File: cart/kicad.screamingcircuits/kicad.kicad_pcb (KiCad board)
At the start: 4 copper layers, 100 x 64 mm, 29 parts, among them J1 Bus_TI994A_Cart, J2 Conn_01x06, U1 MCP1700-3302E_SOT23, U2 S29GL01G-128MB-Flash, U3 GigaCart_CPLD_LC4064

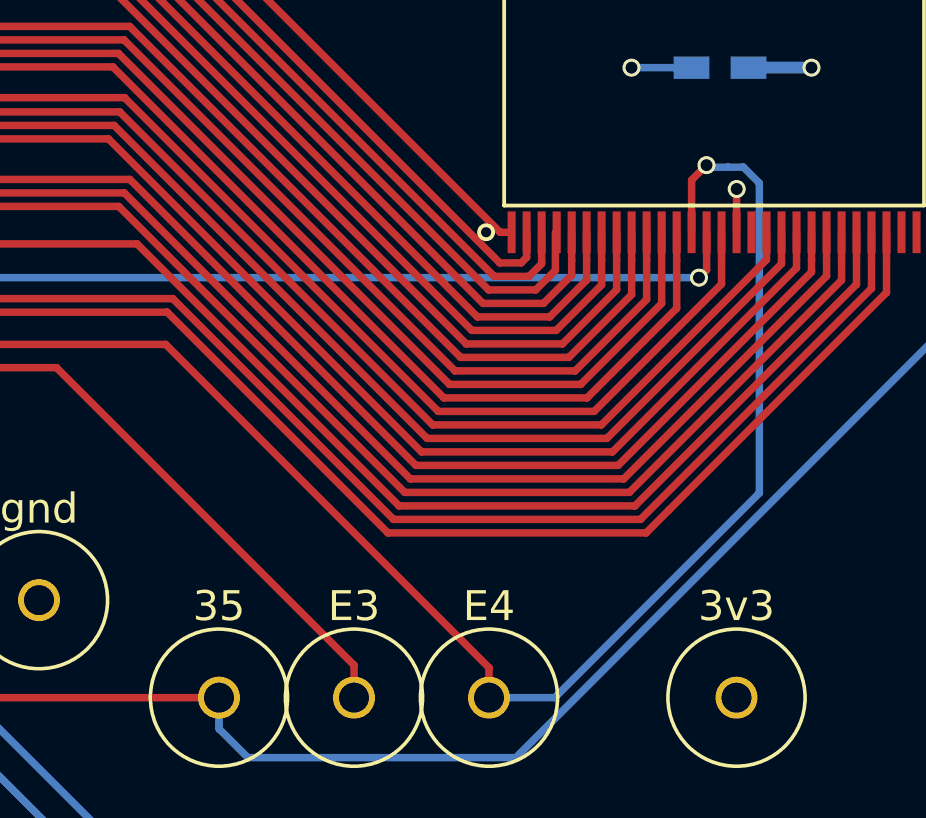
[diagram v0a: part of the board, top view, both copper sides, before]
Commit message: -changed seahorse load back to pull-up (drive OE low) -add checksum to cartWriter (to check ROM checksum) -add a few missing volatiles to cartWriter -fix Dragonostics advanced screen to start on page 16, not page 8 -fix for practice joystick mode not to scan keyboard instead on seahorse board (not shipped broken)
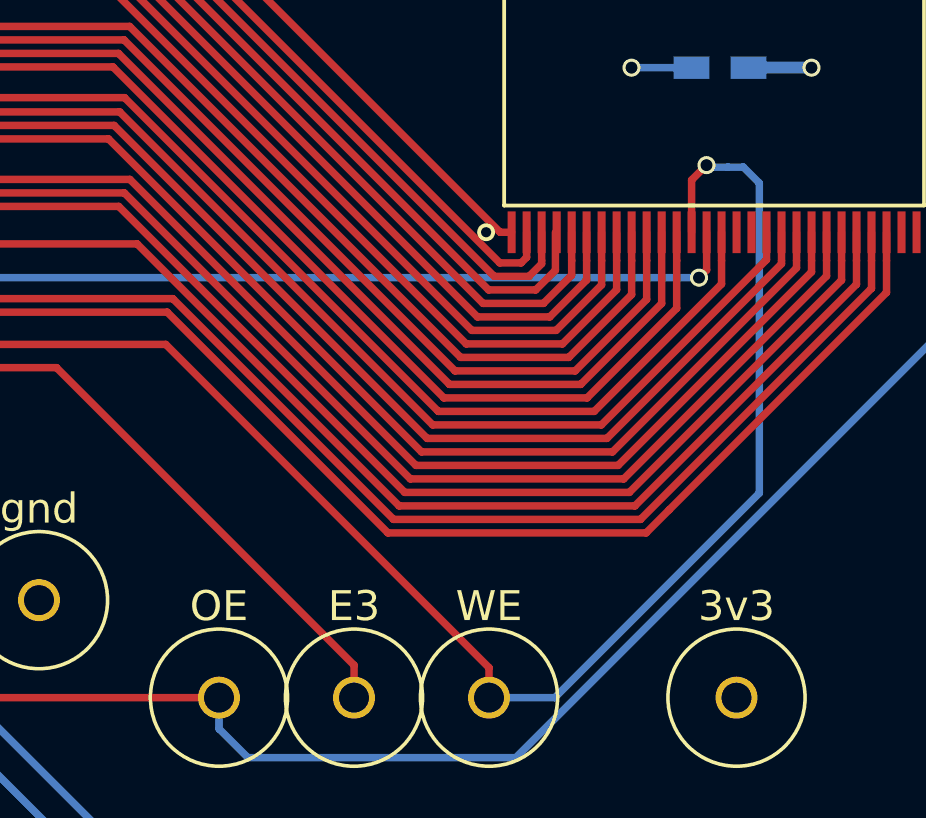
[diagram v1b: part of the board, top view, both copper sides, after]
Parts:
- renumbered 35 to OE, E4 to WE
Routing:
- net GND: track 80.7 -> 79.3 mm, vias 32 -> 31
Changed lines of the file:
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@@
     (thickness 1.6)
     (drawings 18)
-    (tracks 854)
+    (tracks 851)
     (zones 0)
     (modules 29)
@@
     (descr "module 1 pin (ou trou mecanique de percage)")
     (tags DEV)
-    (fp_text reference E4 (at 0 -3.048) (layer F.SilkS)
+    (fp_text reference WE (at 0 -3.048) (layer F.SilkS)
       (effects (font (size 1 1) (thickness 0.15)))
     )
@@
     (descr "module 1 pin (ou trou mecanique de percage)")
     (tags DEV)
-    (fp_text reference 35 (at 0 -3.048) (layer F.SilkS)
+    (fp_text reference OE (at 0 -3.048) (layer F.SilkS)
       (effects (font (size 1 1) (thickness 0.15)))
     )
@@
   (segment (start 121 128) (end 121 121.89) (width 0.4) (layer B.Cu) (net 2) (status 30))
   (via (at 118 118) (size 0.6) (drill 0.4) (layers F.Cu B.Cu) (net 2))
-  (segment (start 180.50216 97.04963) (end 180.506838 97.044952) (width 0.25) (layer F.Cu) (net 2))
-  (via (at 180.506838 97.044952) (size 0.6) (drill 0.4) (layers F.Cu B.Cu) (net 2))
-  (segment (start 180.50216 98.48688) (end 180.50216 97.04963) (width 0.25) (layer F.Cu) (net 2) (status 10))
   (segment (start 179.05 75) (end 177 75) (width 0.4) (layer B.Cu) (net 2) (status 10))
   (via (at 177 75) (size 0.6) (drill 0.4) (layers F.Cu B.Cu) (net 2))

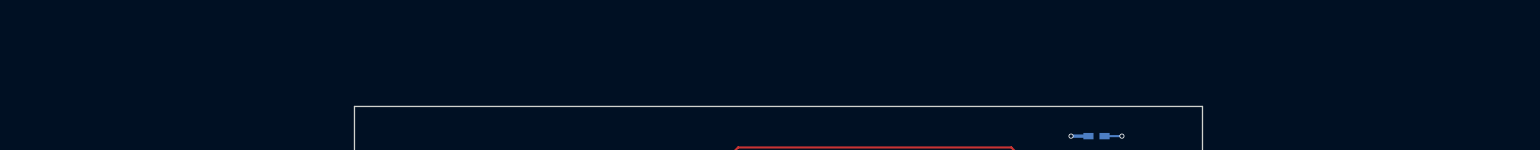
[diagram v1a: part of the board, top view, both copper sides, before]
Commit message: -add CPLD and CartWrite changes for experimental board that manages CE instead of Reset
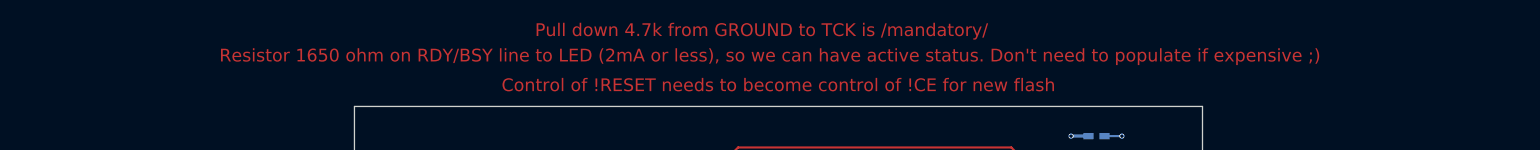
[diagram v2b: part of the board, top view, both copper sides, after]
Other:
- board text added: "Control of !RESET needs to become control of !CE for new flash"
- board text added: "Pull down 4.7k from GROUND to TCK is /mandatory/"
- board text added: "Resistor 1650 ohm on RDY/BSY line to LED (2mA or less), so we can have active status. Don't need to populate if expensive ;)"
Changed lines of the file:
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@@
   (general
     (links 139)
-    (no_connects 0)
-    (area 92 71 193.000001 135.575001)
+    (no_connects 1)
+    (area 66.928572 64.3 216.071428 135.575001)
     (thickness 1.6)
-    (drawings 18)
+    (drawings 21)
     (tracks 851)
     (zones 0)
@@
       (xy -0.00492 6.644475)) (layer B.SilkS) (width 0.01))
   )
+  (gr_text "Pull down 4.7k from GROUND to TCK is /mandatory/" (at 140.5 62.5) (layer F.Cu)
+    (effects (font (size 1.5 1.5) (thickness 0.3)))
+  )
+  (gr_text "Control of !RESET needs to become control of !CE for new flash" (at 142.5 69) (layer F.Cu)
+    (effects (font (size 1.5 1.5) (thickness 0.3)))
+  )
+  (gr_text "Resistor 1650 ohm on RDY/BSY line to LED (2mA or less), so we can have active status. Don't need to populate if expensive ;)" (at 141.5 65.5) (layer F.Cu)
+    (effects (font (size 1.5 1.5) (thickness 0.3)))
+  )
   (gr_text "Pin 16 is WP#, and should be floating to allow programming of the protected top/bottom sector (as per flash chip)." (at 180.5 95.5) (layer Cmts.User)

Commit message: - pushing schematic PDF and all the changes GIT said were there that I don't remember what they were ;)
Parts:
- moved C12 2.24 mm to (178.0, 74.0)
- moved C11 1.00 mm to (179.9, 94.0)
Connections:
- U1 pad 1: GND -> Net-(U1-Pad1)
- U2 pad 16: GND -> Net-(U2-Pad16)
- U2 pad 32: GND -> Net-(J5-Pad1)
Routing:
- net Net-(J5-Pad1): track 35.2 -> 103.6 mm
- net +3V3: track 50.7 -> 52.8 mm
- net Net-(U1-Pad1): track 0.00 -> 0.78 mm
- net GND: track 79.3 -> 79.7 mm, vias 31 -> 32
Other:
- board text added: "Can we rework for 2 layers, and fit Coleco and TI both?"
- board text added: "Pin 16 is ~WP Pin 17 is Ready (out) Pin 32 is ~CE Pin 52 is ~Byte"
- board text added: "resistor is not 1650 see web link for voltage drop!"
- board text removed: "Control of !RESET needs to become control of !CE for new flash"
